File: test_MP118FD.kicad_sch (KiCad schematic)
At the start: 18 parts, among them J1 Screw_Terminal_01x01, J2 Screw_Terminal_01x01, J3 Conn_Coaxial

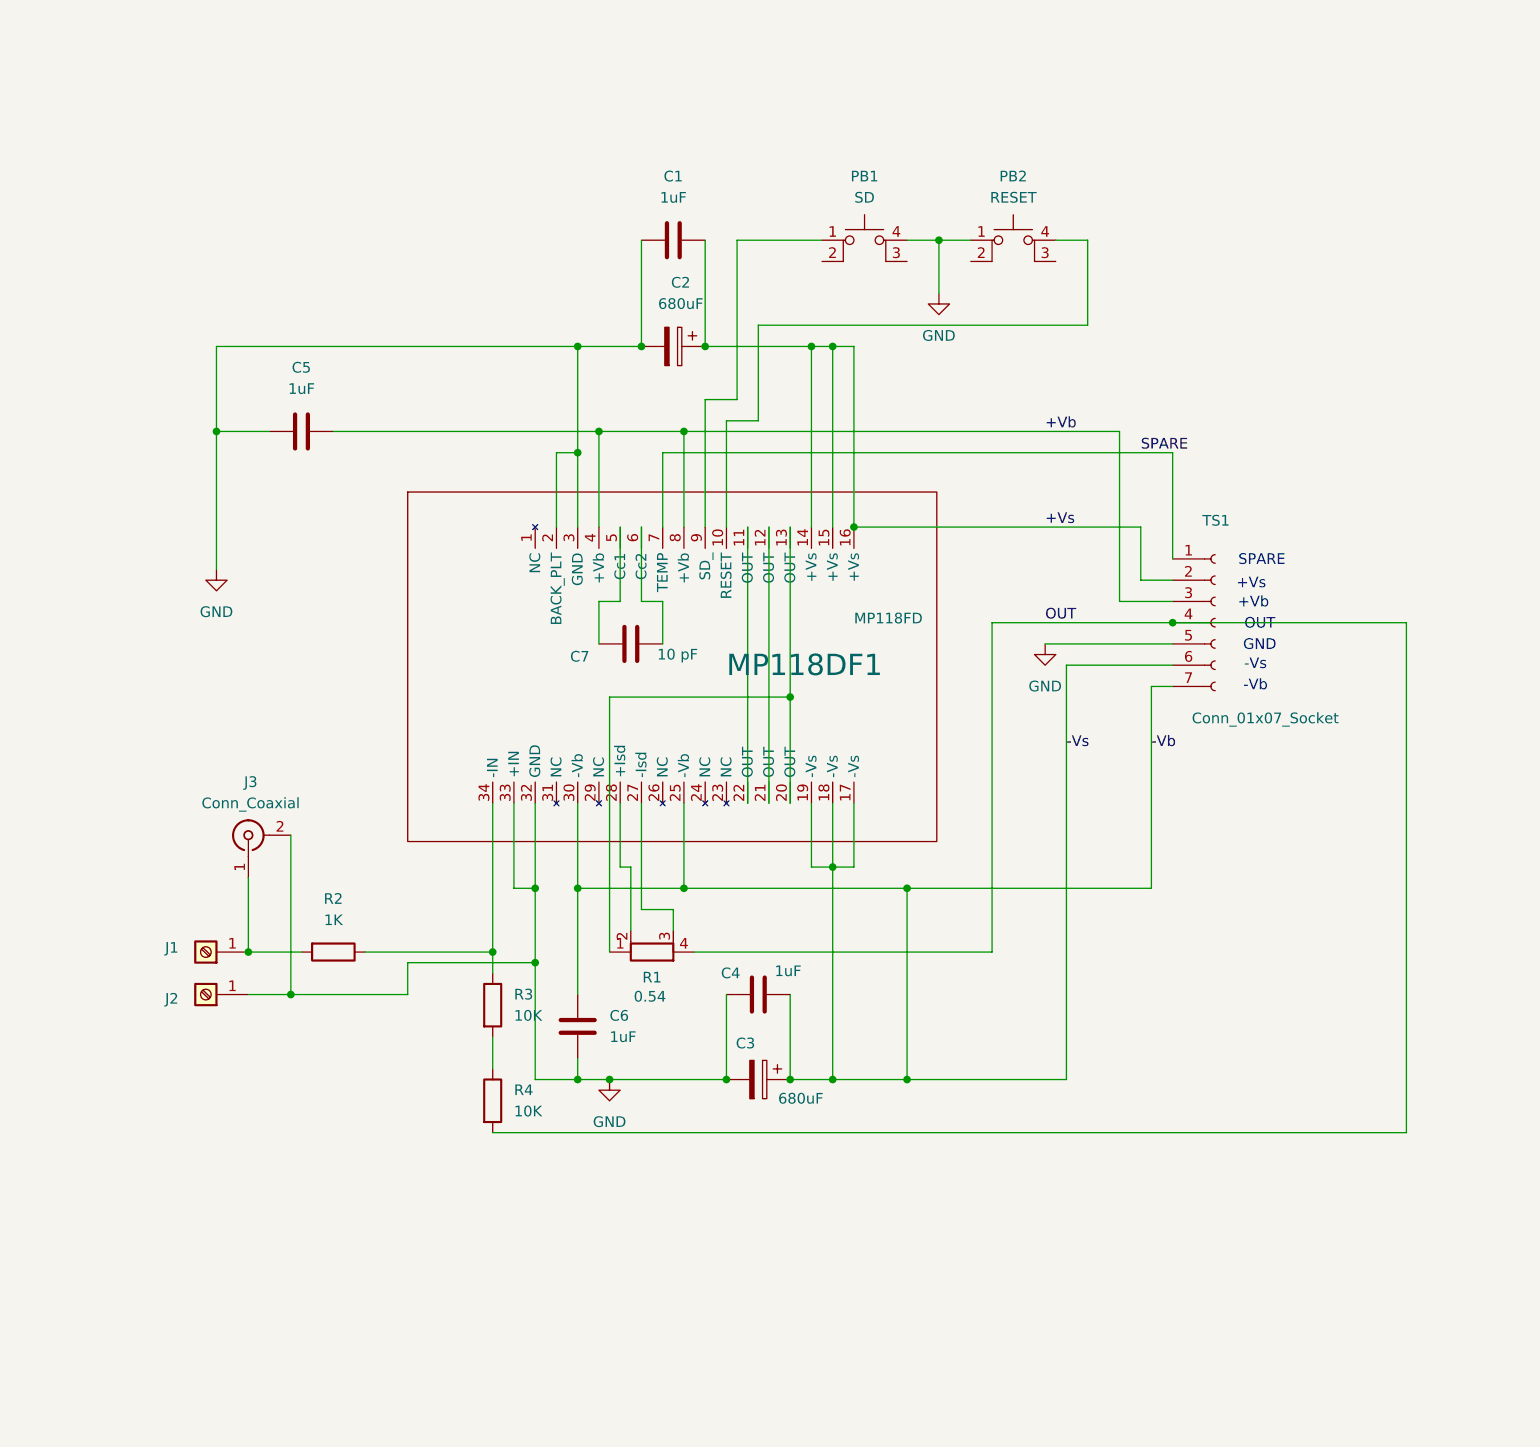
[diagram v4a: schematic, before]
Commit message: Reconfiguración general, arreglos de redes y posiciones mas centradas
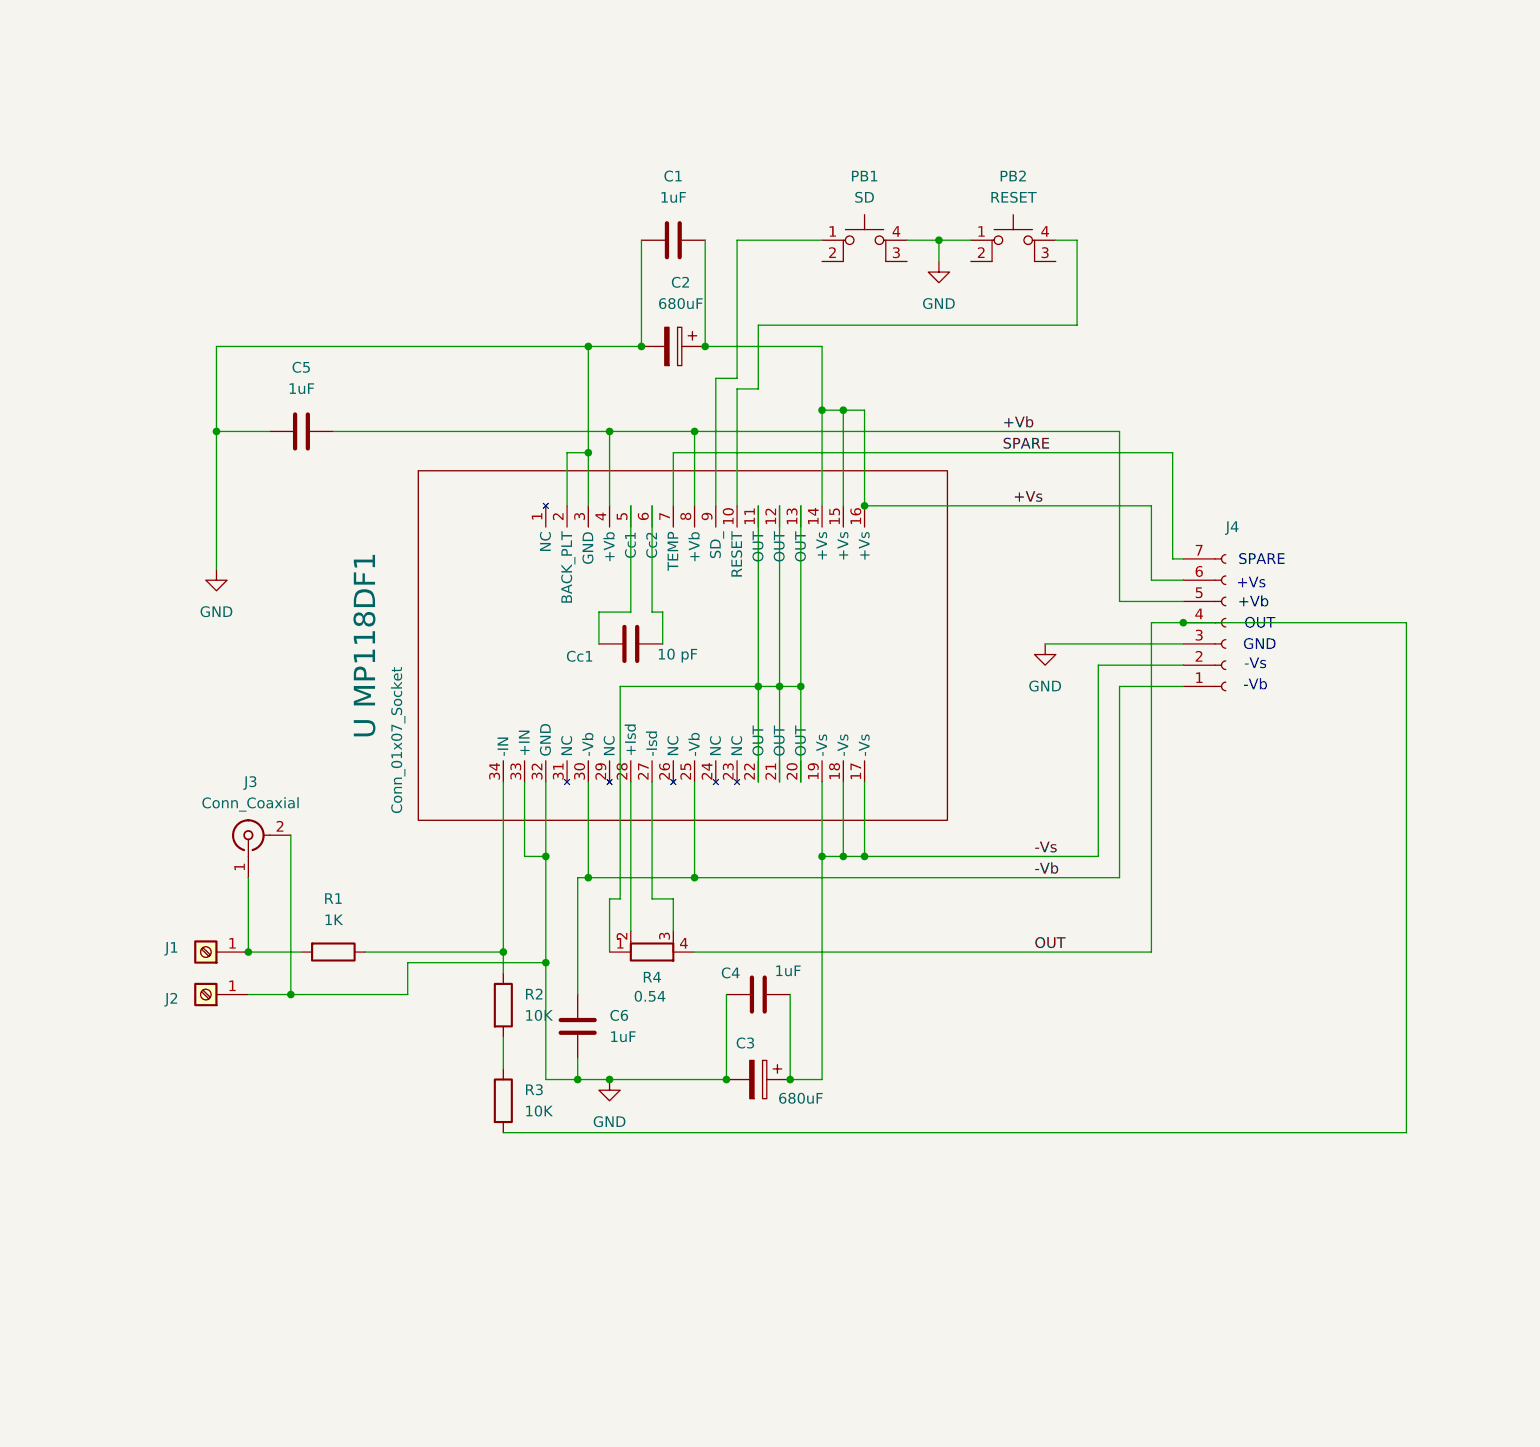
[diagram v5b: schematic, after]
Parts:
- removed MP118DF1: MP118FD, Library:MP118, symbol Apex:MP118FD-girado
- removed TS1: Conn_01x07_Socket, Library:PhoenixContact_SPT_5_7-H-7.5-ZB_1x07_P7.5mm_Horizontal, symbol Apex:Conn_01x07_Socket
- added J4: Conn_01x07_Socket, Library:PhoenixContact_SPT_5_7-H-7.5-ZB_1x07_P7.5mm_Horizontal, symbol Apex:Conn_01x07_Socket
- added U MP118DF1: ~, Library:MP118, symbol Apex:MP118FD-girado
- renumbered C7 to Cc1, R2 to R1, R3 to R2, R4 to R3, R1 to R4
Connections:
- net +Vb: now also J4.5 (Pin_5), U MP118DF1.4 (+Vb), U MP118DF1.8 (+Vb)
- net +Vs: now also J4.6 (Pin_6), U MP118DF1.14 (+Vs), U MP118DF1.15 (+Vs), U MP118DF1.16 (+Vs)
- net -Vb: now also J4.1 (Pin_1), U MP118DF1.25 (-Vb), U MP118DF1.30 (-Vb); no longer C3.1, C4.1
- net GND: now also J4.3 (Pin_3), U MP118DF1.2 (BACK_PLT), U MP118DF1.3 (GND), U MP118DF1.32 (GND), U MP118DF1.33 (+IN)
- net OUT: now also J4.4 (Pin_4)
- net SPARE: now also J4.7 (Pin_7), U MP118DF1.7 (TEMP)
- net at Cc1.1: now also U MP118DF1.6 (Cc2)
- net at Cc1.2: now also U MP118DF1.5 (Cc1)
- net at PB1.1: now also U MP118DF1.9 (SD_)
- net at R1.1, R2.1: now also U MP118DF1.34 (-IN)
- net at PB2.4 (A): now also U MP118DF1.10 (RESET)
- net at R4.1: now also U MP118DF1.11 (OUT), U MP118DF1.12 (OUT), U MP118DF1.13 (OUT), U MP118DF1.20 (OUT), U MP118DF1.21 (OUT), U MP118DF1.22 (OUT)
- net at R4.2: now also U MP118DF1.28 (+Isd)
- net at R4.3: now also U MP118DF1.27 (-Isd)
- new net -Vs: C3.1, C4.1, J4.2 (Pin_2), U MP118DF1.17 (-Vs), U MP118DF1.18 (-Vs), U MP118DF1.19 (-Vs)
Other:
- moved on the sheet: R2, R3

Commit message: Hasta el viernes
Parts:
- added R5: 0, Resistor_THT:R_Axial_DIN0207_L6.3mm_D2.5mm_P7.62mm_Horizontal, symbol Device:R
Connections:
- net +Vb: now also J4.3 (Pin_3); no longer J4.5 (Pin_5)
- net +Vs: now also J4.2 (Pin_2); no longer J4.6 (Pin_6)
- net -Vb: now also J4.7 (Pin_7), R5.2; no longer J4.1 (Pin_1)
- net -Vs: now also J4.6 (Pin_6), R5.1; no longer J4.2 (Pin_2)
- net GND: now also J4.5 (Pin_5), PB1.3 (2), PB2.2; no longer J4.3 (Pin_3)
- net SPARE: now also J4.1 (Pin_1); no longer J4.7 (Pin_7)
- net at PB1.1, U MP118DF1.9 (SD_): now also PB1.2 (1)
- net at PB2.3 (K): now also PB2.4 (A), U MP118DF1.10 (RESET)
- net OUT_0: now reaches R4.1, U MP118DF1.11 (OUT), U MP118DF1.12 (OUT), U MP118DF1.13 (OUT), U MP118DF1.20 (OUT), U MP118DF1.21 (OUT), U MP118DF1.22 (OUT)
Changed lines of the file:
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@@
+	)
+	(junction
+		(at 153.67 39.37)
+		(diameter 0)
+		(color 0 0 0 0)
 	)
 	(junction
@@
 	)
 	(junction
+		(at 171.45 39.37)
+		(diameter 0)
+		(color 0 0 0 0)
+	)
+	(junction
 		(at 146.05 92.71)
 		(diameter 0)
@@
 	)
 	(junction
+		(at 181.61 39.37)
+		(diameter 0)
+		(color 0 0 0 0)
+	)
+	(junction
 		(at 85.09 124.46)
 		(diameter 0)
@@
 	)
 	(junction
+		(at 163.83 39.37)
+		(diameter 0)
+		(color 0 0 0 0)
+	)
+	(junction
 		(at 142.24 139.7)
 		(diameter 0)
@@
 		(color 0 0 0 0)
 	)
+	(junction
+		(at 142.24 115.57)
+		(diameter 0)
+		(color 0 0 0 0)
+	)
 	(wire
 		(pts
@@
 	(wire
 		(pts
+			(xy 142.24 115.57) (xy 138.43 115.57)
+		)
+		(stroke
+			(width 0)
+			(type default)
+		)
+	)
+	(wire
+		(pts
 			(xy 143.51 55.88) (xy 143.51 39.37)
 		)
@@
 	(wire
 		(pts
+			(xy 142.24 113.03) (xy 142.24 115.57)
+		)
+		(stroke
+			(width 0)
+			(type default)
+		)
+	)
+	(wire
+		(pts
 			(xy 148.59 92.71) (xy 148.59 104.14)
 		)
@@
 	(wire
 		(pts
+			(xy 171.45 39.37) (xy 171.45 41.91)
+		)
+		(stroke
+			(width 0)
+			(type default)
+		)
+	)
+	(wire
+		(pts
 			(xy 138.43 71.12) (xy 138.43 62.23)
 		)
@@
 	(wire
 		(pts
-			(xy 189.23 115.57) (xy 138.43 115.57)
+			(xy 189.23 115.57) (xy 142.24 115.57)
 		)
 		(stroke
@@
 	(wire
 		(pts
+			(xy 181.61 39.37) (xy 181.61 41.91)
+		)
+		(stroke
+			(width 0)
+			(type default)
+		)
+	)
+	(wire
+		(pts
 			(xy 153.67 104.14) (xy 153.67 113.03)
 		)
@@
 	(wire
 		(pts
+			(xy 149.86 113.03) (xy 153.67 113.03)
+		)
+		(stroke
+			(width 0)
+			(type default)
+		)
+	)
+	(wire
+		(pts
 			(xy 115.57 124.46) (xy 115.57 127)
 		)
@@
 		(pts
 			(xy 133.35 118.11) (xy 133.35 104.14)
+		)
+		(stroke
+			(width 0)
+			(type default)
+		)
+	)
+	(wire
+		(pts
+			(xy 153.67 39.37) (xy 153.67 41.91)
+		)
+		(stroke
+			(width 0)
+			(type default)
+		)
+	)
+	(wire
+		(pts
+			(xy 163.83 39.37) (xy 163.83 41.91)
 		)
 		(stroke
@@
 	(label "+Vb"
 		(at 175.26 62.23 0)
+		(effects
+			(font
+				(size 1.27 1.27)
+			)
+			(justify left bottom)
+		)
+	)
+	(label "OUT_0"
+		(at 151.13 85.09 0)
 		(effects
 			(font
@@
 	)
 	(symbol
+		(lib_id "Device:R")
+		(at 146.05 113.03 270)
+		(unit 1)
+		(exclude_from_sim no)
+		(in_bom yes)
+		(on_board yes)
+		(dnp no)
+		(property "Reference" "R5"
+			(at 146.05 116.84 90)
+			(effects
+				(font
+					(size 1.27 1.27)
+				)
+			)
+		)
+		(property "Value" "0"
+			(at 146.05 119.38 90)
+			(effects
+				(font
+					(size 1.27 1.27)
+				)
+			)
+		)
+		(property "Footprint" "Resistor_THT:R_Axial_DIN0207_L6.3mm_D2.5mm_P7.62mm_Horizontal"
+			(at 146.05 111.252 90)
+			(effects
+				(font
+					(size 1.27 1.27)
+				)
+				(hide yes)
+			)
+		)
+		(property "Datasheet" "~"
+			(at 146.05 113.03 0)
+			(effects
+				(font
+					(size 1.27 1.27)
+				)
+				(hide yes)
+			)
+		)
+		(property "Description" "Resistor"
+			(at 146.05 113.03 0)
+			(effects
+				(font
+					(size 1.27 1.27)
+				)
+				(hide yes)
+			)
+		)
+		(property "Proveedor" "RS:707-7666"
+			(at 146.05 113.03 0)
+			(effects
+				(font
+					(size 1.27 1.27)
+				)
+				(hide yes)
+			)
+		)
+		(property "Precio" "1,31 €. 10 unidades"
+			(at 146.05 113.03 0)
+			(effects
+				(font
+					(size 1.27 1.27)
+				)
+				(hide yes)
+			)
+		)
+		(pin "1"
+		)
+		(pin "2"
+		)
+		(instances
+			(project "test_MP118FD"
+				(path "/0ca9cec8-9e01-403d-ae88-5180092a6e53"
+					(reference "R5")
+					(unit 1)
+				)
+			)
+		)
+	)
+	(symbol
+		(lib_name "SW_MEC_5E_1")
 		(lib_id "Switch:SW_MEC_5E")
 		(at 158.75 41.91 0)
@@
 		(dnp no)
 		(property "Reference" "J4"
-			(at 201.93 73.66 0)
-			(effects
-				(font
+			(at 201.93 71.12 0)
+			(effects
+				(font
